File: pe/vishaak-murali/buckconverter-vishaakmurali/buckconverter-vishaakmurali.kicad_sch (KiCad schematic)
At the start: 9 parts, among them J1 VIN_IN, J2 VOUT_5V, U1 TPS54202DDC

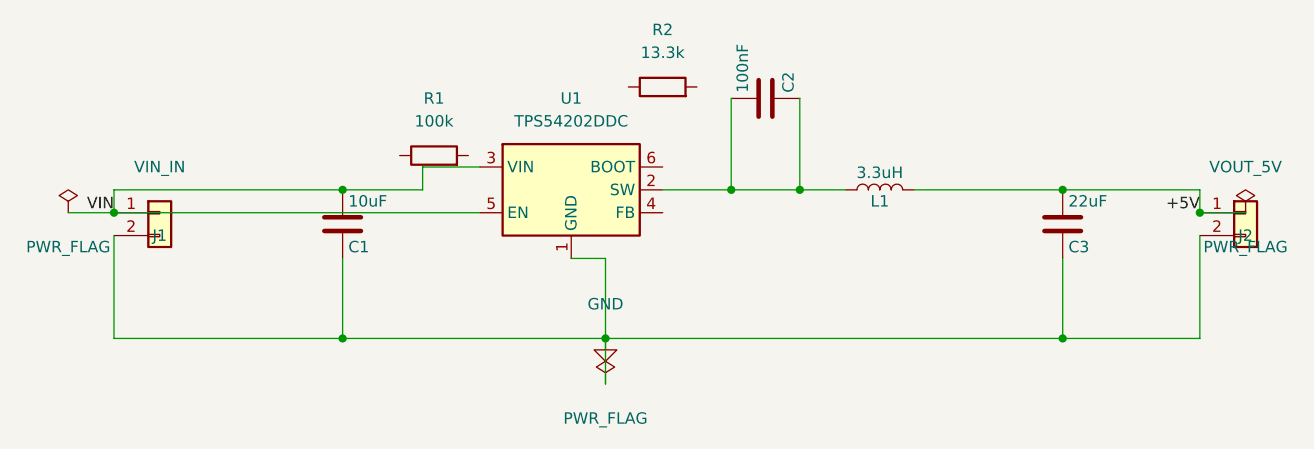
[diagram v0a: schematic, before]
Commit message: fix buck schematic wiring and route pcb
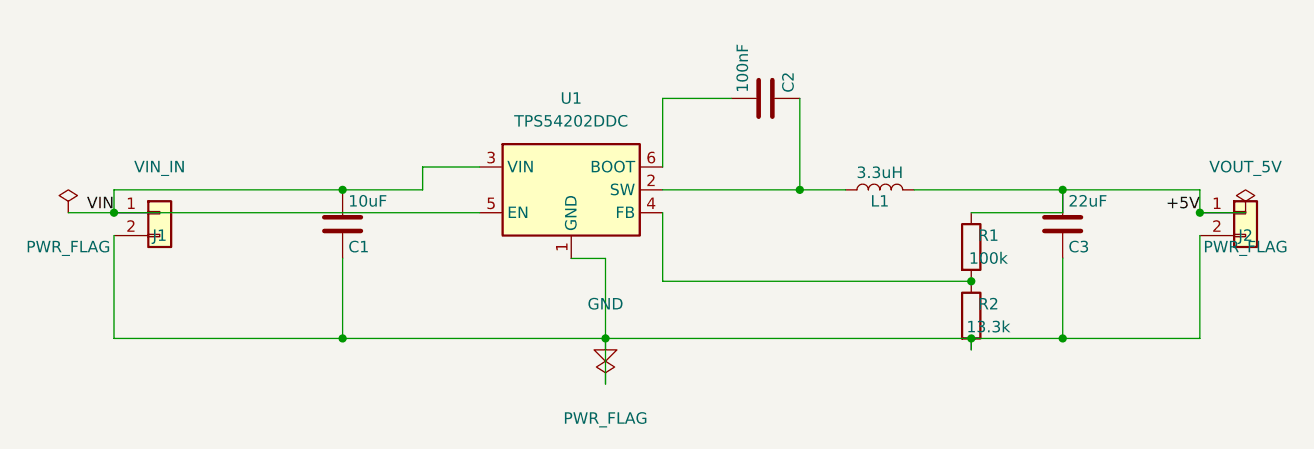
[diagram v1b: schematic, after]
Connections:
- net +5V: now also R1.1
- net GND: now also R2.2
- net at R1.2: now also R2.1, U1.4 (FB)
- net at C2.2, L1.1, U1.2 (SW): no longer C2.1
- net at U1.6 (BOOT): now also C2.1
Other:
- moved on the sheet: R1, R2
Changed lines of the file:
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@@
-	)
-	(junction
-		(at 138.43 97.79)
-		(diameter 0)
-		(color 0 0 0 0)
 	)
 	(junction
@@
 	(wire
 		(pts
-			(xy 138.43 87.63) (xy 138.43 97.79)
-		)
-		(stroke
-			(width 0)
-			(type default)
-		)
-	)
-	(wire
-		(pts
 			(xy 190.5 100.33) (xy 195.58 100.33)
 		)
@@
 	(wire
 		(pts
-			(xy 130.81 97.79) (xy 138.43 97.79)
+			(xy 130.81 97.79) (xy 146.05 97.79)
 		)
 		(stroke
@@
 		(pts
 			(xy 175.26 97.79) (xy 190.5 97.79)
-		)
-		(stroke
-			(width 0)
-			(type default)
-		)
-	)
-	(wire
-		(pts
-			(xy 138.43 97.79) (xy 146.05 97.79)
 		)
 		(stroke
@@
 	(symbol
 		(lib_id "Device:R")
-		(at 105.41 93.98 90)
+		(at 165.1 104.14 0)
 		(unit 1)
 		(body_style 1)
@@
 		(fields_autoplaced yes)
 		(property "Reference" "R1"
-			(at 105.41 87.63 90)
+			(at 167.005 102.87 0)
 			(show_name no)
 			(do_not_autoplace no)
@@
 		)
 		(property "Value" "100k"
-			(at 105.41 90.17 90)
+			(at 167.005 105.41 0)
 			(show_name no)
 			(do_not_autoplace no)
@@
 	(symbol
 		(lib_id "Device:R")
-		(at 130.81 86.36 90)
+		(at 165.1 111.76 0)
 		(unit 1)
 		(body_style 1)
@@
 		(fields_autoplaced yes)
 		(property "Reference" "R2"
-			(at 130.81 80.01 90)
+			(at 167.005 110.49 0)
 			(show_name no)
 			(do_not_autoplace no)
@@
 		)
 		(property "Value" "13.3k"
-			(at 130.81 82.55 90)
+			(at 167.005 113.03 0)
 			(show_name no)
 			(do_not_autoplace no)
@@
 		)
 	)
+	(wire
+		(pts
+			(xy 138.43 87.63) (xy 130.81 87.63)
+		)
+		(stroke
+			(width 0)
+			(type default)
+		)
+	)
+	(wire
+		(pts
+			(xy 130.81 87.63) (xy 130.81 95.25)
+		)
+		(stroke
+			(width 0)
+			(type default)
+		)
+	)
+	(wire
+		(pts
+			(xy 165.10 100.33) (xy 175.26 100.33)
+		)
+		(stroke
+			(width 0)
+			(type default)
+		)
+	)
+	(wire
+		(pts
+			(xy 175.26 100.33) (xy 175.26 97.79)
+		)
+		(stroke
+			(width 0)
+			(type default)
+		)
+	)
+	(wire
+		(pts
+			(xy 165.10 107.95) (xy 130.81 107.95)
+		)
+		(stroke
+			(width 0)
+			(type default)
+		)
+	)
+	(wire
+		(pts
+			(xy 130.81 107.95) (xy 130.81 100.33)
+		)
+		(stroke
+			(width 0)
+			(type default)
+		)
+	)
+	(junction
+		(at 165.10 107.95)
+		(diameter 0)
+		(color 0 0 0 0)
+	)
+	(wire
+		(pts
+			(xy 165.10 115.57) (xy 165.10 114.30)
+		)
+		(stroke
+			(width 0)
+			(type default)
+		)
+	)
+	(junction
+		(at 165.10 114.30)
+		(diameter 0)
+		(color 0 0 0 0)
+	)
 	(sheet_instances
